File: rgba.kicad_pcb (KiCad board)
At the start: 4 copper layers, 45.5 x 26.5 mm, 78 parts, among them J1 USB C CHG, J10 UART_RTS, J11 Screw 1, J12 Screw 2, J2 BATT CONN, J3 UART_GND, J4 R SPK OUT, J5 L SPK OUT, J6 UART_CTS, J7 UART_VBUS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

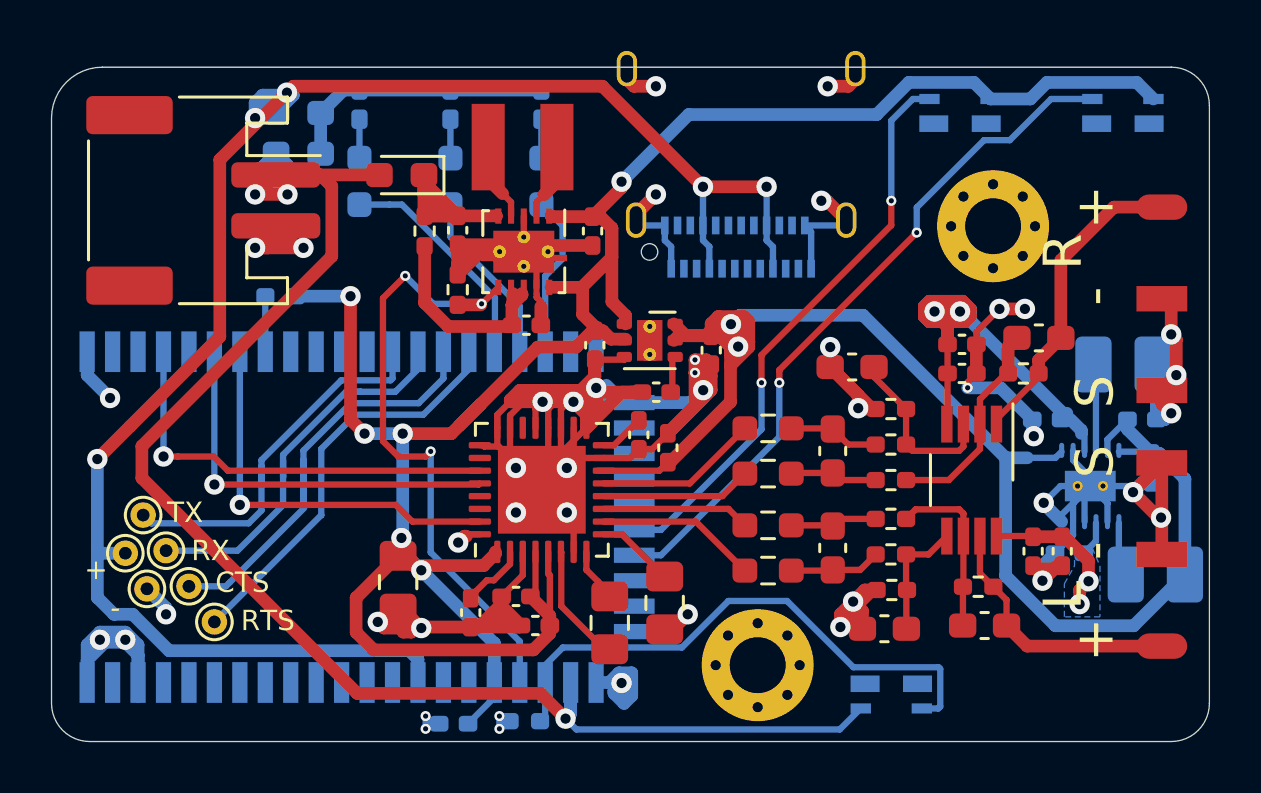
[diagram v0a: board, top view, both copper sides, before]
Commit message: new 3.3v voltage regulator and updated a few footprints
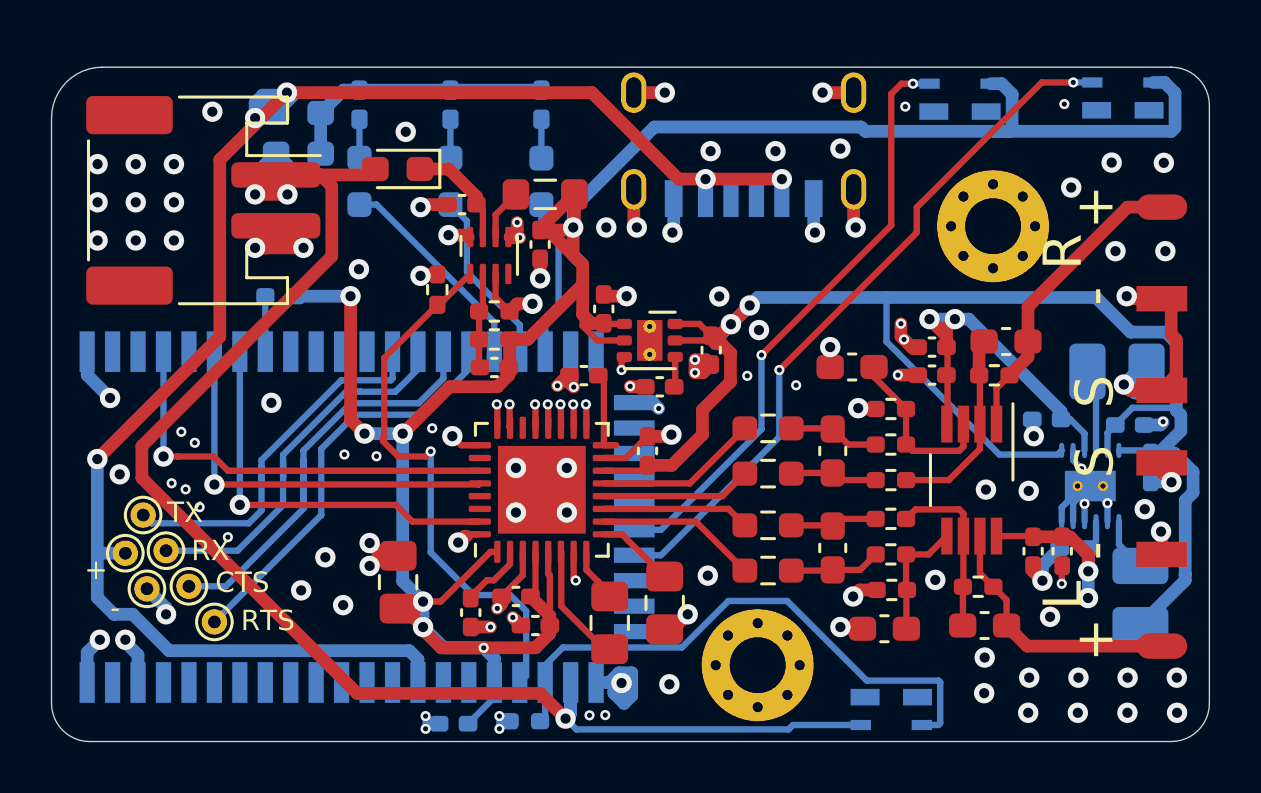
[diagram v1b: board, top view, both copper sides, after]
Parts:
- removed the R30 at (93.7, 95.4)
- added R31: 453k, Resistor_SMD:R_0402_1005Metric_Pad0.72x0.64mm_HandSolder, F.Cu at (96.4, 99.7)
- added R32: 100k, Resistor_SMD:R_0402_1005Metric_Pad0.72x0.64mm_HandSolder, F.Cu at (96.4, 98.6)
- C30: value 0.1uF -> 10uF
- C31: value 0.1uF -> 120pF
- J1: value USB C CHG -> USB_C_Receptacle_USB2.0; footprint Connector_USB:USB_C_Receptacle_Amphenol_12401610E4-2A -> Connector_USB:USB_C_Receptacle_UJC-HP-3-SMT-TR
- L30: value 2.2uH -> 470nH; footprint Inductor_SMD:L_TDK_VLS3012 -> Inductor_SMD:L_0805_2012Metric_Pad1.05x1.20mm_HandSolder
- U3: value TPS63001 -> TPS62821DLC; footprint Package_SON:Texas_DRC0010J_ThermalVias -> Package_DFN_QFN:Texas_VSON-HR-8_1.5x2mm_P0.5mm
- moved C26 3.17 mm to (99.9, 101.1), turned to 0 degrees
- moved C32 2.13 mm to (98.2, 96.0)
- moved C31 2.08 mm to (96.4, 100.8), turned to 180 degrees
- moved L30 2.06 mm to (98.4, 94.0)
- moved J1 1.90 mm to (106.2, 90.0)
- moved C40 1.47 mm to (100.7, 98.5), turned to 90 degrees
- moved U3 1.37 mm to (96.2, 96.4), turned to 90 degrees
- moved C612 1.30 mm to (116.5, 99.8)
- moved C601 1.18 mm to (113.6, 100.0), turned to 0 degrees
- moved C603 1.18 mm to (113.6, 101.1), turned to 0 degrees
- moved R615 1.14 mm to (116.0, 101.1)
- moved C30 1.02 mm to (95.1, 94.4), turned to 180 degrees
- moved L50 1.01 mm to (121.8, 109.8), turned to 90 degrees
- moved C27 0.81 mm to (102.4, 104.1)
- moved R30 0.80 mm to (94.2, 97.7)
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- renumbered R31 to R30
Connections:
- C31 pad 1: Net-(C31-Pad1) -> +3V3
- C31 pad 2: GND -> Net-(C31-Pad2)
- L30 pad 2: Net-(L30-Pad2) -> +3V3
- U3 pad 1: +3V3 -> +1V8
- U3 pad 2: Net-(L30-Pad2) -> Net-(C31-Pad2)
- U3 pad 4: Net-(L30-Pad1) -> Net-(U3-Pad4)
- U3 pad 5: Net-(C30-Pad1) -> GND
- U3 pad 6: +1V8 -> Net-(L30-Pad1)
- U3 pad 7: Net-(C31-Pad1) -> Net-(C30-Pad1)
- U3 pad 8: Net-(C31-Pad1) -> GND
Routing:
- net GND: track 214.7 -> 101.9 mm, vias 44 -> 131
- net -5VA: track 26.5 -> 14.6 mm
- net Net-(C30-Pad1): track 12.4 -> 4.37 mm
- net Net-(C31-Pad1): track 7.94 -> 0.00 mm
- net VBUS: track 70.5 -> 65.7 mm
- net Net-(C31-Pad2): track 0.00 -> 3.75 mm
- net +1V8: track 24.9 -> 21.8 mm, vias 3 -> 1
- net Net-(L30-Pad2): track 3.04 -> 0.00 mm
- net +3V3: track 96.8 -> 98.7 mm, vias 6 -> 7
- net Net-(C26-Pad2): track 1.78 -> 3.31 mm
- net +3.3VA: track 61.7 -> 63.2 mm
- net Net-(L30-Pad1): track 3.08 -> 2.01 mm
- net PIO6: track 22.8 -> 23.6 mm
- net Net-(C612-Pad1): track 8.43 -> 7.72 mm
- net LED_CHG: track 9.04 -> 8.44 mm
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- removed copper zone on B.Cu, net +5VA

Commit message: start working on new regulator
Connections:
- J4 pad 3: GND -> Net-(J4-Pad3)
- J5 pad 3: GND -> Net-(J5-Pad3)
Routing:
- net GND: track 101.9 -> 95.3 mm, vias 131 -> 128
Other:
- board text added: "bluetooth audio"
- board text added: "cts"
- board text added: "designed by"
- board text added: "gray olson"
- board text added: "reasonably good"
- board text added: "rev 1.0"
- board text added: "rgba"
- board text added: "rts"
- board text added: "rx"
- board text added: "tx"
- board text removed: "CTS"
- board text removed: "RTS"
- board text removed: "RX"
- board text removed: "TX"

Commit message: rev 1.1
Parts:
- removed C32: 10uF, Capacitor_SMD:C_0402_1005Metric_Pad0.74x0.62mm_HandSolder
- removed R31: 453k, Resistor_SMD:R_0402_1005Metric_Pad0.72x0.64mm_HandSolder
- removed R32: 100k, Resistor_SMD:R_0402_1005Metric_Pad0.72x0.64mm_HandSolder
- C31: value 120pF -> 10uF
- J1: value USB_C_Receptacle_USB2.0 -> CHARGE CONN; footprint Connector_USB:USB_C_Receptacle_UJC-HP-3-SMT-TR -> rgba:USB_C_Receptacle_UJC-HP-3-SMT-TR
- J11: footprint MountingHole:MountingHole_2.2mm_M2_Pad_Via -> rgba:MountingHole_1.2mm_M1_Pad
- J12: value Screw 2 -> Screw 1; footprint MountingHole:MountingHole_2.2mm_M2_Pad_Via -> rgba:MountingHole_1.2mm_M1_Pad
- J2: footprint Connector_JST:JST_PH_S2B-PH-SM4-TB_1x02-1MP_P2.00mm_Horizontal -> Connector_JST:JST_ACH_BM02B-ACHSS-GAN-ETF_1x02-1MP_P1.20mm_Vertical
- J4, J5: footprint Connector_Wire:SolderWire-0.1sqmm_1x03_P3.6mm_D0.4mm_OD1mm -> rgba:SolderWire_AudioOut_1x03_P2.0mm
- L30: value 470nH -> 4.7uH; footprint Inductor_SMD:L_0805_2012Metric_Pad1.05x1.20mm_HandSolder -> Inductor_SMD:L_1008_2520Metric_Pad1.43x2.20mm_HandSolder
- LED1: renamed from D3; value RED -> ORNG
- LED3: renamed from D5; value GREEN -> WHITE
- R1, R2, R3, R610, R611, R620, R621: value 1k -> 1K
- R10, R11, R30: value 100k -> 100K
- R22, R614, R615, R624: value 68 -> 68R
- R612, R613, R622, R623: value 4.7k -> 4.7K
- SW1: value POWER/PLAY/PAUSE -> Switch_RA; footprint SamacSys_Parts:TL4110AF160Q -> rgba:TL4110AF160Q
- SW2: value VOL+/NEXT -> Switch_RA; footprint SamacSys_Parts:TL4110AF160Q -> rgba:TL4110AF160Q
- SW3: value VOL-/BACK -> Switch_RA; footprint SamacSys_Parts:TL4110AF160Q -> rgba:TL4110AF160Q
- U2: footprint Package_DFN_QFN:QFN-32-1EP_5x5mm_P0.5mm_EP3.45x3.45mm -> rgba:QFN-32-1EP_5x5mm_P0.5mm_EP3.45x3.45mm
- U3: value TPS62821DLC -> TPS62849DLCR; footprint Package_DFN_QFN:Texas_VSON-HR-8_1.5x2mm_P0.5mm -> rgba:VSON-8_1.5x2mm_P0.5mm
- U4: footprint Package_SON:WSON-6-1EP_2x2mm_P0.65mm_EP1x1.6mm_ThermalVias -> rgba:WSON-6-1EP_2x2mm_P0.65mm_EP1x1.6mm_ThermalVias
- U6: footprint Package_SO:VSSOP-8_3.0x3.0mm_P0.65mm -> rgba:VSSOP-8_3.0x3.0mm_P0.65mm
- moved SW3 31.5 mm to (104.2, 115.5), turned to 180 degrees
- moved SW2 26.5 mm to (115.8, 115.5), turned to 180 degrees
- moved J12 10.4 mm to (105.6, 95.5)
- moved C50 8.65 mm to (113.5, 104.7)
- moved C51 8.65 mm to (112.7, 103.1)
- moved L51 8.65 mm to (112.2, 101.0)
- moved C52 8.65 mm to (110.5, 107.9)
- moved C53 8.65 mm to (109.5, 102.8)
- moved U5 8.65 mm to (111.2, 105.5)
- moved J1 7.52 mm to (112.6, 94.0)
- moved J4 7.31 mm to (117.5, 99.7)
- moved L50 7.28 mm to (115.5, 106.1), turned to 270 degrees
- moved J5 5.50 mm to (117.5, 113.6)
- moved C31 5.02 mm to (96.8, 95.8), turned to 90 degrees
- moved D30 4.54 mm to (89.7, 96.5), turned to 270 degrees
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- renumbered D4 to LED2
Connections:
- net PIO6 renamed VOL+_NEXT
- net PIO7 renamed VOL-_PREV
- C31 pad 2: Net-(C31-Pad2) -> GND
- U3 pad 1: +1V8 -> GND
- U3 pad 2: Net-(C31-Pad2) -> Net-(C30-Pad1)
- U3 pad 4: Net-(U3-Pad4) -> +1V8
- U3 pad 6: Net-(L30-Pad1) -> GND
- U3 pad 7: Net-(C30-Pad1) -> Net-(L30-Pad1)
- U3 pad 8: GND -> +3V3
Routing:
- net +3.3VA: track 63.2 -> 45.4 mm
- net GND: track 95.3 -> 78.3 mm, vias 128 -> 81
- net VBAT: track 68.7 -> 52.5 mm
- net VOL-_PREV: track 27.8 -> 13.1 mm, vias 2 -> 0
- net -5VA: track 14.6 -> 8.01 mm, vias 2 -> 1
- net +3V3: track 98.7 -> 92.5 mm, vias 7 -> 10
- net VOL+_NEXT: track 23.6 -> 18.1 mm, vias 2 -> 0
- net LED_CONN: track 6.91 -> 2.37 mm
- net OUT_R: track 12.2 -> 7.95 mm
- net I2S_DATA: track 15.7 -> 11.8 mm
- net I2S_CLK: track 16.8 -> 13.0 mm
- net I2S_LRCK: track 15.7 -> 11.9 mm
- net VREG_IN: track 22.6 -> 18.8 mm, vias 0 -> 2
- net Net-(C31-Pad2): track 3.75 -> 0.00 mm
- net Net-(D1-Pad1): track 10.6 -> 14.1 mm
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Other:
- board size 45.5 x 26.5 mm -> 40 x 22.5 mm
- board text added: "rev 1.1"
- board text removed: "rev 1.0"

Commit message: update readme, gerbers, bom
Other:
- board size 40 x 22.5 mm -> 40 x 23 mm
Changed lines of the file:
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@@
     (fp_line (start 2.12 -1.35) (end 2.12 1.35) (layer F.CrtYd) (width 0.05))
     (fp_line (start 2.12 1.35) (end -2.12 1.35) (layer F.CrtYd) (width 0.05))
-    (pad 2 smd roundrect (at 1.1625 0 90) (size 1.425 2.2) (layers F.Cu F.Paste F.Mask) (roundrect_rratio 0.175439)
+    (pad 2 smd roundrect (at 1.1625 0 90) (size 1.425 2.2) (layers F.Cu F.Paste F.Mask) (roundrect_rratio 0.1754385964912281)
       (net 1 +3V3))
-    (pad 1 smd roundrect (at -1.1625 0 90) (size 1.425 2.2) (layers F.Cu F.Paste F.Mask) (roundrect_rratio 0.175439)
+    (pad 1 smd roundrect (at -1.1625 0 90) (size 1.425 2.2) (layers F.Cu F.Paste F.Mask) (roundrect_rratio 0.1754385964912281)
       (net 32 "Net-(L30-Pad1)"))
     (model ${KISYS3DMOD}/Inductor_SMD.3dshapes/L_1008_2520Metric.wrl
@@
     (fp_line (start 2.12 1.35) (end 2.12 -1.35) (layer B.CrtYd) (width 0.05))
     (fp_line (start 2.12 -1.35) (end -2.12 -1.35) (layer B.CrtYd) (width 0.05))
-    (pad 2 smd roundrect (at 1.1625 0) (size 1.425 2.2) (layers B.Cu B.Paste B.Mask) (roundrect_rratio 0.175439)
-      (net 2 GND))
-    (pad 1 smd roundrect (at -1.1625 0) (size 1.425 2.2) (layers B.Cu B.Paste B.Mask) (roundrect_rratio 0.175439)
+    (pad 2 smd roundrect (at 1.1625 0) (size 1.425 2.2) (layers B.Cu B.Paste B.Mask) (roundrect_rratio 0.1754385964912281)
+      (net 2 GND))
+    (pad 1 smd roundrect (at -1.1625 0) (size 1.425 2.2) (layers B.Cu B.Paste B.Mask) (roundrect_rratio 0.1754385964912281)
       (net 34 "Net-(L51-Pad1)"))
     (model ${KISYS3DMOD}/Inductor_SMD.3dshapes/L_1008_2520Metric.wrl
@@
       (effects (font (size 0.62 0.62) (thickness 0.09)) (justify mirror))
     )
-    (pad 1 smd roundrect (at -1.1625 0 270) (size 1.425 2.2) (layers B.Cu B.Paste B.Mask) (roundrect_rratio 0.175439)
+    (pad 1 smd roundrect (at -1.1625 0 270) (size 1.425 2.2) (layers B.Cu B.Paste B.Mask) (roundrect_rratio 0.1754385964912281)
       (net 8 +3.3VA))
-    (pad 2 smd roundrect (at 1.1625 0 270) (size 1.425 2.2) (layers B.Cu B.Paste B.Mask) (roundrect_rratio 0.175439)
+    (pad 2 smd roundrect (at 1.1625 0 270) (size 1.425 2.2) (layers B.Cu B.Paste B.Mask) (roundrect_rratio 0.1754385964912281)
       (net 33 "Net-(L50-Pad2)"))
     (model ${KISYS3DMOD}/Inductor_SMD.3dshapes/L_1008_2520Metric.wrl
@@
     (fp_line (start 1.88 -0.98) (end 1.88 0.98) (layer F.CrtYd) (width 0.05))
     (fp_line (start 1.88 0.98) (end -1.88 0.98) (layer F.CrtYd) (width 0.05))
-    (pad 2 smd roundrect (at 1.0375 0 90) (size 1.175 1.45) (layers F.Cu F.Paste F.Mask) (roundrect_rratio 0.212766)
+    (pad 2 smd roundrect (at 1.0375 0 90) (size 1.175 1.45) (layers F.Cu F.Paste F.Mask) (roundrect_rratio 0.2127659574468085)
       (net 6 "Net-(C25-Pad2)"))
-    (pad 1 smd roundrect (at -1.0375 0 90) (size 1.175 1.45) (layers F.Cu F.Paste F.Mask) (roundrect_rratio 0.212766)
+    (pad 1 smd roundrect (at -1.0375 0 90) (size 1.175 1.45) (layers F.Cu F.Paste F.Mask) (roundrect_rratio 0.2127659574468085)
       (net 2 GND))
     (model ${KISYS3DMOD}/Capacitor_SMD.3dshapes/C_0805_2012Metric.wrl
@@
     (fp_line (start 1.88 -0.98) (end 1.88 0.98) (layer F.CrtYd) (width 0.05))
     (fp_line (start 1.88 0.98) (end -1.88 0.98) (layer F.CrtYd) (width 0.05))
-    (pad 2 smd roundrect (at 1.0375 0 270) (size 1.175 1.45) (layers F.Cu F.Paste F.Mask) (roundrect_rratio 0.212766)
+    (pad 2 smd roundrect (at 1.0375 0 270) (size 1.175 1.45) (layers F.Cu F.Paste F.Mask) (roundrect_rratio 0.2127659574468085)
       (net 4 "Net-(C24-Pad2)"))
-    (pad 1 smd roundrect (at -1.0375 0 270) (size 1.175 1.45) (layers F.Cu F.Paste F.Mask) (roundrect_rratio 0.212766)
+    (pad 1 smd roundrect (at -1.0375 0 270) (size 1.175 1.45) (layers F.Cu F.Paste F.Mask) (roundrect_rratio 0.2127659574468085)
       (net 5 "Net-(C24-Pad1)"))
     (model ${KISYS3DMOD}/Capacitor_SMD.3dshapes/C_0805_2012Metric.wrl
@@
     (fp_line (start 1.88 -0.98) (end 1.88 0.98) (layer F.CrtYd) (width 0.05))
     (fp_line (start 1.88 0.98) (end -1.88 0.98) (layer F.CrtYd) (width 0.05))
-    (pad 2 smd roundrect (at 1.0375 0 90) (size 1.175 1.45) (layers F.Cu F.Paste F.Mask) (roundrect_rratio 0.212766)
-      (net 2 GND))
-    (pad 1 smd roundrect (at -1.0375 0 90) (size 1.175 1.45) (layers F.Cu F.Paste F.Mask) (roundrect_rratio 0.212766)
+    (pad 2 smd roundrect (at 1.0375 0 90) (size 1.175 1.45) (layers F.Cu F.Paste F.Mask) (roundrect_rratio 0.2127659574468085)
+      (net 2 GND))
+    (pad 1 smd roundrect (at -1.0375 0 90) (size 1.175 1.45) (layers F.Cu F.Paste F.Mask) (roundrect_rratio 0.2127659574468085)
       (net 1 +3V3))
     (model ${KISYS3DMOD}/Capacitor_SMD.3dshapes/C_0805_2012Metric.wrl
@@
     (effects (font (size 0.8 0.8) (thickness 0.153)))
   )
-  (gr_text rgba (at 86 101.05) (layer F.SilkS)
+  (gr_text rgba (at 86.5 101.05) (layer F.SilkS)
     (effects (font (size 3 3) (thickness 0.5)))
   )
@@
   (gr_arc (start 81 114) (end 79.5 114) (angle -90) (layer Edge.Cuts) (width 0.05))
   (gr_arc (start 118 114) (end 118 115.5) (angle -90) (layer Edge.Cuts) (width 0.05))
-  (gr_arc (start 118 94.5) (end 119.5 94.5) (angle -90) (layer Edge.Cuts) (width 0.05))
-  (gr_arc (start 81.5 95) (end 81.5 93) (angle -90) (layer Edge.Cuts) (width 0.05))
-  (gr_line (start 119.5 94.5) (end 119.5 114) (layer Edge.Cuts) (width 0.05))
+  (gr_arc (start 118 94) (end 119.5 94) (angle -90) (layer Edge.Cuts) (width 0.05))
+  (gr_arc (start 81.5 94.5) (end 81.5 92.5) (angle -90) (layer Edge.Cuts) (width 0.05))
+  (gr_line (start 119.5 94) (end 119.5 114) (layer Edge.Cuts) (width 0.05))
   (gr_line (start 81 115.5) (end 118 115.5) (layer Edge.Cuts) (width 0.05))
-  (gr_line (start 81.5 93) (end 118 93) (layer Edge.Cuts) (width 0.05))
-  (gr_line (start 79.5 114) (end 79.5 95) (layer Edge.Cuts) (width 0.05))
+  (gr_line (start 81.5 92.5) (end 118 92.5) (layer Edge.Cuts) (width 0.05))
+  (gr_line (start 79.5 114) (end 79.5 94.5) (layer Edge.Cuts) (width 0.05))
   (via (at 103.45 113.95) (size 0.8) (drill 0.4) (layers F.Cu B.Cu) (net 1))
   (via (at 117.4 111.6) (size 0.8) (drill 0.4) (layers F.Cu B.Cu) (net 2))
@@
     (polygon
       (pts
-        (xy 119.5 115.5) (xy 79 115.5) (xy 79 93) (xy 119.5 93.1)
+        (xy 119.5 115.5) (xy 79 115.5) (xy 79 92.45) (xy 119.5 92.55)
       )
     )
@@
     (polygon
       (pts
-        (xy 119.5 115.5) (xy 79 115.5) (xy 79 93) (xy 119.5 93)
+        (xy 119.5 115.5) (xy 79 115.5) (xy 79 92.5) (xy 119.5 92.5)
       )
     )
